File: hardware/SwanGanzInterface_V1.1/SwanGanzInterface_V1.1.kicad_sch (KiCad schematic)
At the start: 0 parts

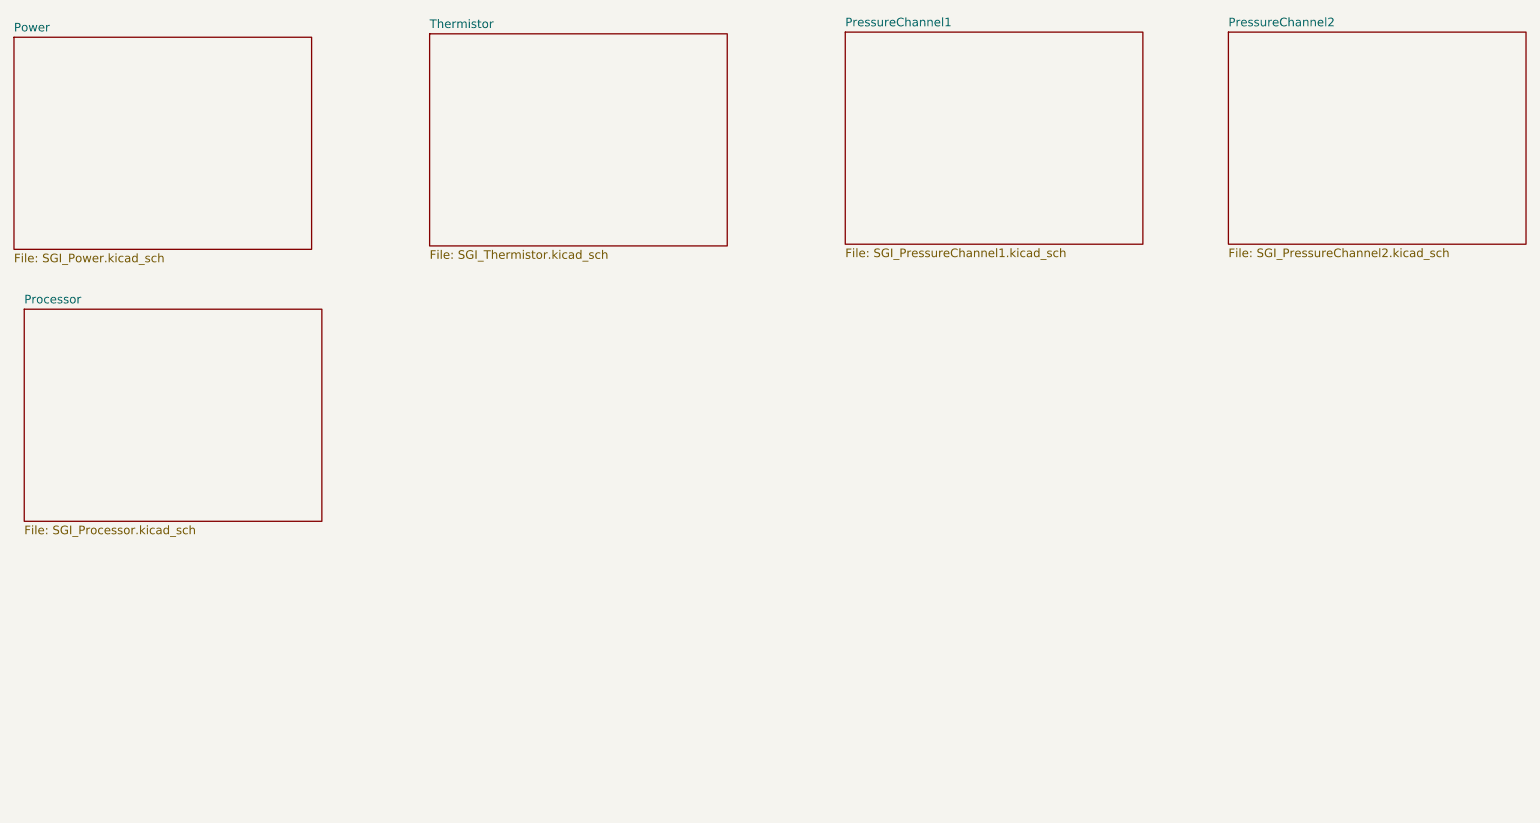
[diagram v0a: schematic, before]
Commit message: Pin Allocation, updated schematic with new pins, reassigned
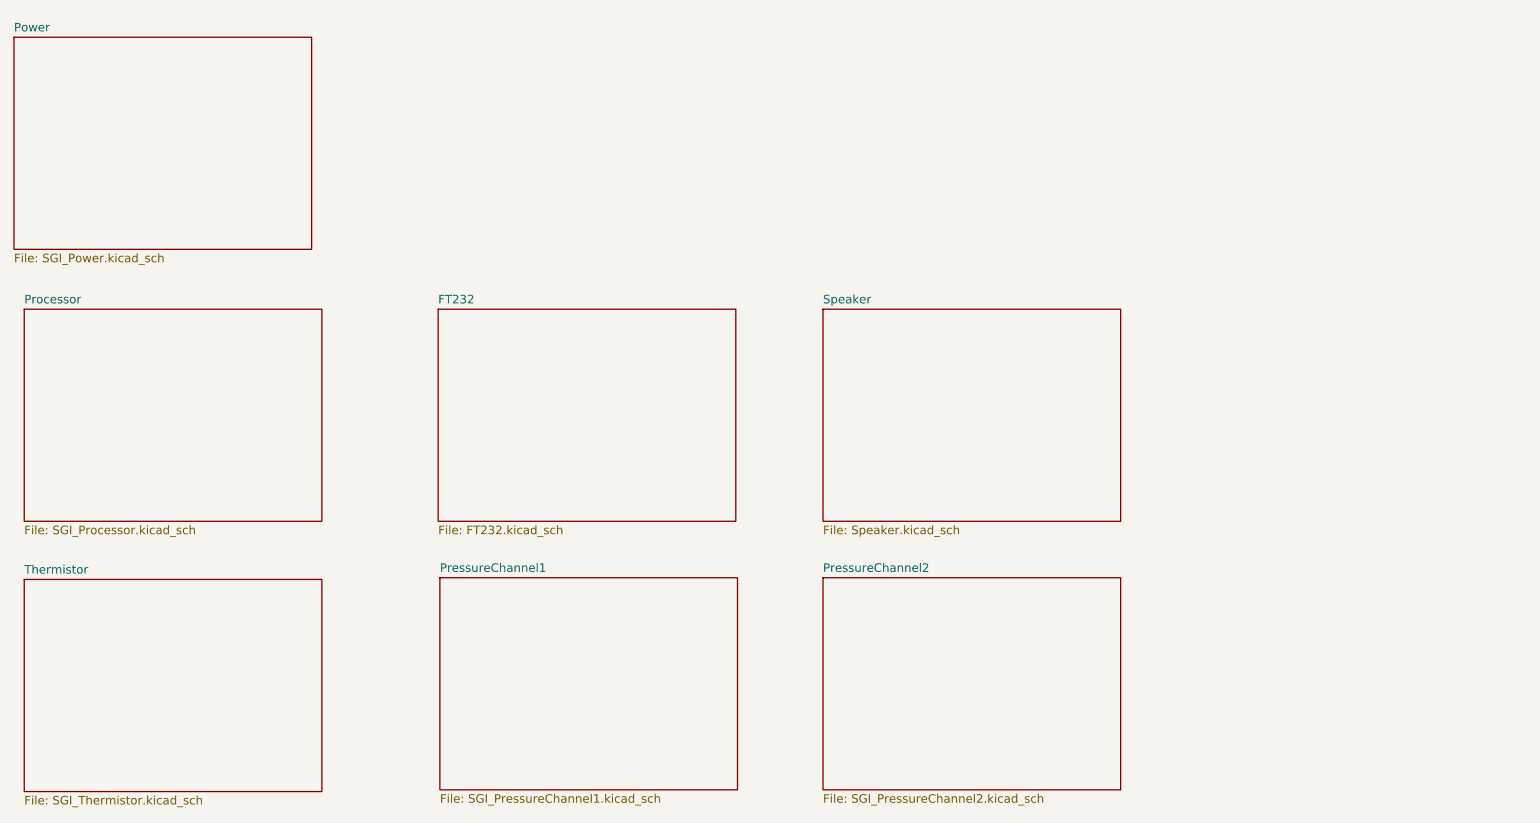
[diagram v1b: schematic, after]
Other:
- added sheet FT232 (FT232.kicad_sch)
- added sheet Speaker (Speaker.kicad_sch)
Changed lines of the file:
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@@
 	)
 	(sheet
-		(at 96.774 33.02)
+		(at 98.044 73.914)
+		(size 44.196 31.496)
+		(exclude_from_sim no)
+		(in_bom yes)
+		(on_board yes)
+		(dnp no)
+		(fields_autoplaced yes)
+		(stroke
+			(width 0.1524)
+			(type solid)
+		)
+		(fill
+			(color 216 174 255 1.0000)
+		)
+		(property "Sheetname" "FT232"
+			(at 98.044 73.2024 0)
+			(effects
+				(font
+					(size 1.27 1.27)
+				)
+				(justify left bottom)
+			)
+		)
+		(property "Sheetfile" "FT232.kicad_sch"
+			(at 98.044 105.9946 0)
+			(effects
+				(font
+					(size 1.27 1.27)
+				)
+				(justify left top)
+			)
+		)
+		(instances
+			(project "SwanGanzInterface_V1.1"
+				(path "/4e9a6e30-f660-472b-9696-bea1f34b4545"
+					(page "7")
+				)
+			)
+		)
+	)
+	(sheet
+		(at 36.576 114.046)
 		(size 44.196 31.496)
 		(exclude_from_sim no)
@@
 		)
 		(property "Sheetname" "Thermistor"
-			(at 96.774 32.3084 0)
+			(at 36.576 113.3344 0)
 			(effects
 				(font
@@
 		)
 		(property "Sheetfile" "SGI_Thermistor.kicad_sch"
-			(at 96.774 65.1006 0)
+			(at 36.576 146.1266 0)
 			(effects
 				(font
@@
 	)
 	(sheet
-		(at 158.496 32.766)
+		(at 98.298 113.792)
 		(size 44.196 31.496)
 		(exclude_from_sim no)
@@
 		)
 		(property "Sheetname" "PressureChannel1"
-			(at 158.496 32.0544 0)
+			(at 98.298 113.0804 0)
 			(effects
 				(font
@@
 		)
 		(property "Sheetfile" "SGI_PressureChannel1.kicad_sch"
-			(at 158.496 64.8466 0)
+			(at 98.298 145.8726 0)
 			(effects
 				(font
@@
 	)
 	(sheet
-		(at 215.392 32.766)
+		(at 155.194 113.792)
 		(size 44.196 31.496)
 		(exclude_from_sim no)
@@
 		)
 		(property "Sheetname" "PressureChannel2"
-			(at 215.392 32.0544 0)
+			(at 155.194 113.0804 0)
 			(effects
 				(font
@@
 		)
 		(property "Sheetfile" "SGI_PressureChannel2.kicad_sch"
-			(at 215.392 64.8466 0)
+			(at 155.194 145.8726 0)
 			(effects
 				(font
@@
 				)
 			)
+		)
+	)
+	(sheet
+		(at 155.194 73.914)
+		(size 44.196 31.496)
+		(exclude_from_sim no)
+		(in_bom yes)
+		(on_board yes)
+		(dnp no)
+		(fields_autoplaced yes)
+		(stroke
+			(width 0.1524)
+			(type solid)
+		)
+		(fill
+			(color 129 226 255 1.0000)
+		)
+		(property "Sheetname" "Speaker"
+			(at 155.194 73.2024 0)
+			(effects
+				(font
+					(size 1.27 1.27)
+				)
+				(justify left bottom)
+			)
+		)
+		(property "Sheetfile" "Speaker.kicad_sch"
+			(at 155.194 105.9946 0)
+			(effects
+				(font
+					(size 1.27 1.27)
+				)
+				(justify left top)
+			)
+		)
+		(instances
+			(project "SwanGanzInterface_V1.1"
+				(path "/4e9a6e30-f660-472b-9696-bea1f34b4545"
+					(page "8")
+				)
+			)

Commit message: Started converting things to use touch screen chip
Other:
- sheet FT232 renamed AuxiliaryDevices
- sheet AuxiliaryDevices: file FT232.kicad_sch -> AuxiliaryDevices.kicad_sch
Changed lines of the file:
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@@
 			(color 216 174 255 1.0000)
 		)
-		(property "Sheetname" "FT232"
+		(property "Sheetname" "AuxiliaryDevices"
 			(at 98.044 73.2024 0)
 			(effects
@@
 			)
 		)
-		(property "Sheetfile" "FT232.kicad_sch"
+		(property "Sheetfile" "AuxiliaryDevices.kicad_sch"
 			(at 98.044 105.9946 0)
 			(effects
